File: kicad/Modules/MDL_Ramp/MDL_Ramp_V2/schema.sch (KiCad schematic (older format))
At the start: 10 parts, among them U1 OP37G, U2 DAC08

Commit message: update MDL_Pulser_V2
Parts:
- U2: value DAC08 -> DAC0800
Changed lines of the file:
@@
 P 5000 3450
 F 0 "U2" H 4550 4150 50  0000 L CNN
-F 1 "DAC08" H 5200 4150 50  0000 L CNN
+F 1 "DAC0800" H 5200 4150 50  0000 L CNN
 F 2 "" H 5000 3450 50  0000 C CNN
 F 3 "" H 5000 3450 50  0000 C CNN
@@
 $EndComp
 $Comp
-L GND #PWR06
+L GND #PWR05
 U 1 1 57599160
 P 6700 2800
-F 0 "#PWR06" H 6700 2550 50  0001 C CNN
+F 0 "#PWR05" H 6700 2550 50  0001 C CNN
 F 1 "GND" H 6700 2650 50  0000 C CNN
 F 2 "" H 6700 2800 50  0000 C CNN
@@
 	6700 3250 6800 3250
 $Comp
-L GND #PWR07
+L GND #PWR06
 U 1 1 575EADC9
 P 5700 3250
-F 0 "#PWR07" H 5700 3000 50  0001 C CNN
+F 0 "#PWR06" H 5700 3000 50  0001 C CNN
 F 1 "GND" H 5700 3100 50  0000 C CNN
 F 2 "" H 5700 3250 50  0000 C CNN
@@
 Connection ~ 8100 3350
 $Comp
-L GND #PWR08
+L GND #PWR07
 U 1 1 575ED2D2
 P 8100 3950
-F 0 "#PWR08" H 8100 3700 50  0001 C CNN
+F 0 "#PWR07" H 8100 3700 50  0001 C CNN
 F 1 "GND" H 8100 3800 50  0000 C CNN
 F 2 "" H 8100 3950 50  0000 C CNN

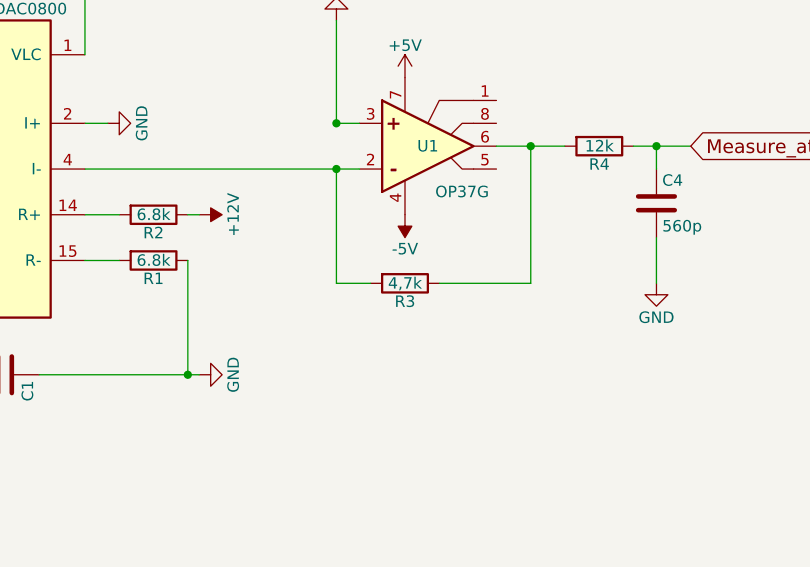
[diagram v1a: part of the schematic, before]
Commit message: adding software modules (flowcharts)
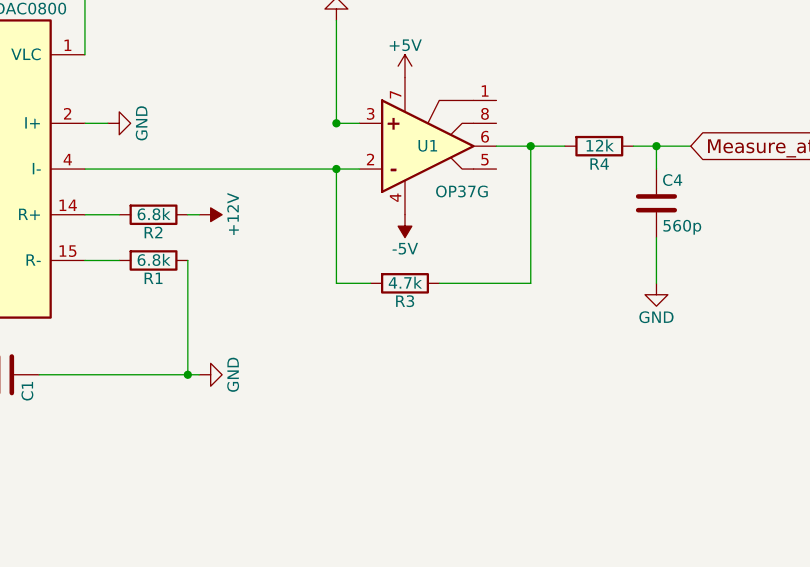
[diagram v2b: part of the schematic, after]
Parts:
- R3: value 4,7k -> 4.7k
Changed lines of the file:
@@
 P 7000 3950
 F 0 "R3" V 7080 3950 50  0000 C CNN
-F 1 "4,7k" V 7000 3950 50  0000 C CNN
+F 1 "4.7k" V 7000 3950 50  0000 C CNN
 F 2 "" V 6930 3950 50  0000 C CNN
 F 3 "" H 7000 3950 50  0000 C CNN
